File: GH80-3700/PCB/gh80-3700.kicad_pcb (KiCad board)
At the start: 2 copper layers, 91.8 x 149.1 mm, 86 parts, among them J1 HRO-TYPE-C-31-M-12, J2 ISP, J3 USB, J4 EXP, J5 RGB, K1 KEYSW, K10 KEYSW, K11 KEYSW, K12 KEYSW, K13 KEYSW, K14 KEYSW, K15 KEYSW, K16 KEYSW, K16-1 KEYSW, K17 KEYSW, K18 KEYSW, K19 KEYSW, K2 KEYSW, K20 KEYSW, K21 KEYSW, K21-1 KEYSW, K22 KEYSW, K23 KEYSW, K24 KEYSW, K24-1 KEYSW, K3 KEYSW, K4 KEYSW, K5 KEYSW, K6 KEYSW, K7 KEYSW, K8 KEYSW, K9 KEYSW, SW1 SW_PUSH, SW2 Rotary_Encoder_Switch, U1 ATmega32U4, U2 USBLC6-2SC6, X1 XTAL_GND

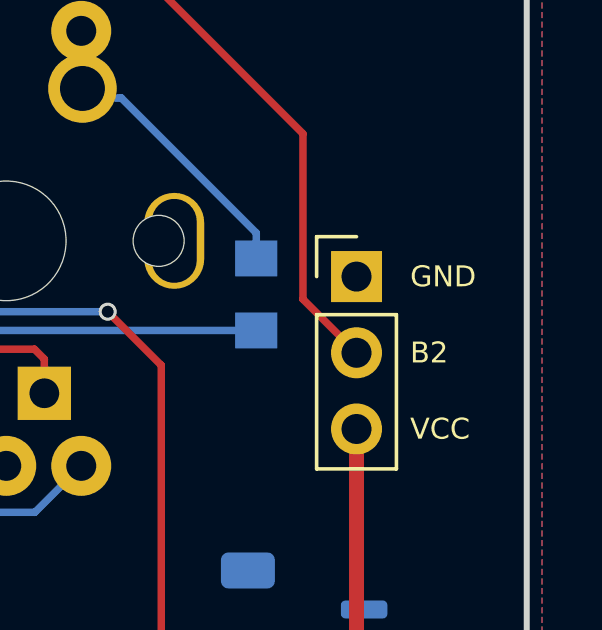
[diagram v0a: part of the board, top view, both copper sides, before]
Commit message: Add website logo/remove maartenwut
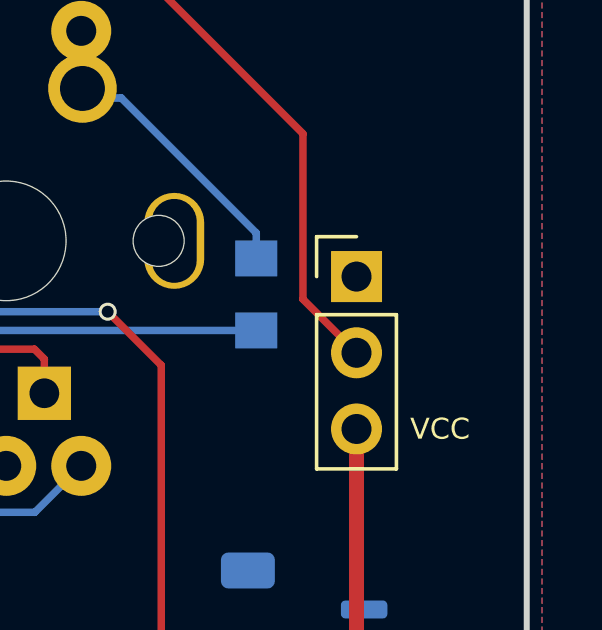
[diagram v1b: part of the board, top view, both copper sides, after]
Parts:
- added G***: LOGO, Keeb_components:logo_new, B.Cu at (8.70, 3.57)
- moved G*** 8.63 mm to (28.9, 3.57)
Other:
- net class Default removed
- net class VCC removed
- board text added: "rev 2.1"
- board text removed: "B2"
- board text removed: "Designed by Maartenwut"
- board text removed: "rev 2"
